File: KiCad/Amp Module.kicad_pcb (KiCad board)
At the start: 2 copper layers, 13.2 x 16.3 mm, 2 parts

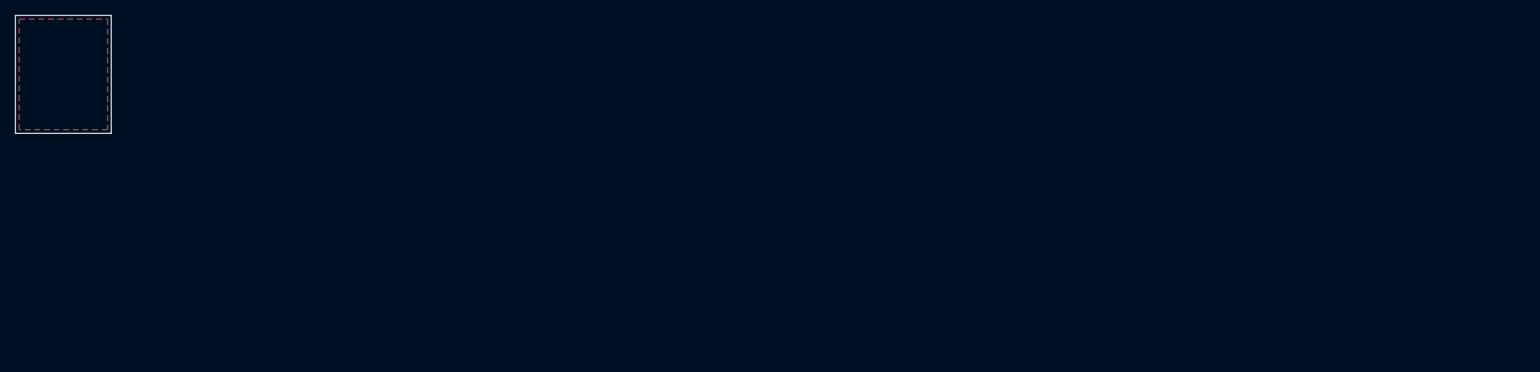
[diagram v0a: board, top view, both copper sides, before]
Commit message: finished PCB with TL12
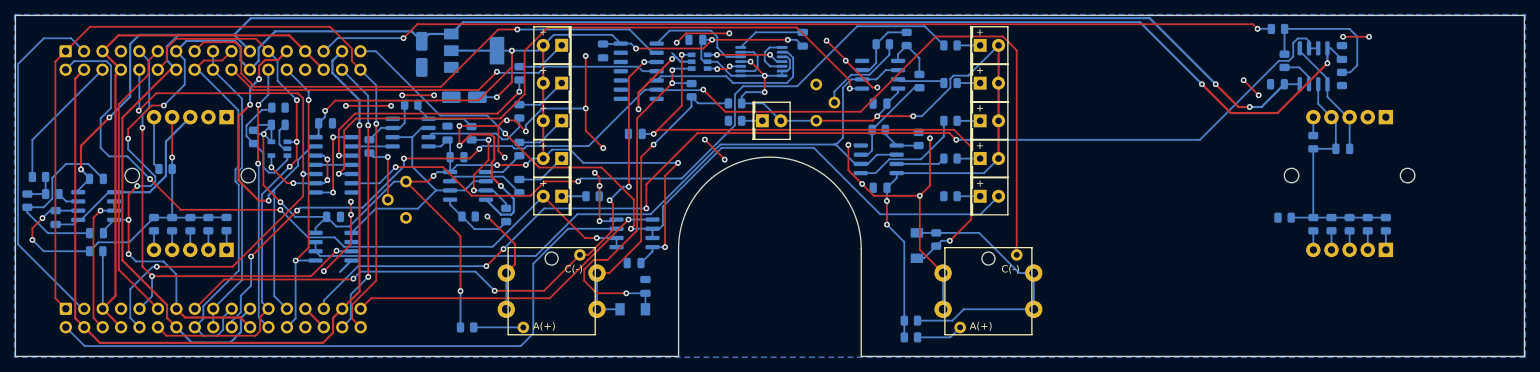
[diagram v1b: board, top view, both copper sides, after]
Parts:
- removed G***: LOGO, AmpModule:Fingerprint_SolderMask
- removed G***: LOGO, AmpModule:Fingerprint
- added C1: 22p, Capacitor_SMD:C_0805_2012Metric, B.Cu at (20.8, 43.1)
- added C10: 1u, Capacitor_SMD:C_0805_2012Metric, B.Cu at (100.7, 31.6)
- added C11: 0.1uF, Capacitor_SMD:C_0805_2012Metric, B.Cu at (100.5, 49.4)
- added C12: 0.1uF, Capacitor_SMD:C_0805_2012Metric, B.Cu at (123.8, 18.5)
- added C13: 0.1uF, Capacitor_SMD:C_0805_2012Metric, B.Cu at (96.2, 20.1)
- added C14: 0.1uF, Capacitor_SMD:C_0805_2012Metric, B.Cu at (51.5, 30.3)
- added C15: 0.1uF, Capacitor_SMD:C_0805_2012Metric, B.Cu at (59.1, 43.0)
- added C16: 0.1uF, Capacitor_SMD:C_0805_2012Metric, B.Cu at (58.0, 30.1)
- added C17: 0.1uF, Capacitor_SMD:C_0805_2012Metric, B.Cu at (74.8, 31.5)
- added C18: 0.1uF, Capacitor_SMD:C_0805_2012Metric, B.Cu at (76.1, 34.8)
- added C19: 0.1uF, Capacitor_SMD:C_0805_2012Metric, B.Cu at (134.4, 39.0)
- added C2: 22p, Capacitor_SMD:C_0805_2012Metric, B.Cu at (198.2, 33.6)
- added C20: 0.1uF, Capacitor_SMD:C_0805_2012Metric, B.Cu at (134.4, 27.4)
- added C21: 0.1uF, Capacitor_SMD:C_0805_2012Metric, B.Cu at (109.0, 18.6)
- added C3: 0.1uF, Capacitor_SMD:C_0805_2012Metric, B.Cu at (26.4, 37.8)
- added C4: 0.1uF, Capacitor_SMD:C_0805_2012Metric, B.Cu at (189.2, 24.7)
- added C5: 0.1uF, Capacitor_SMD:C_0805_2012Metric, B.Cu at (26.4, 45.3)
- added C6: 0.1uF, Capacitor_SMD:C_0805_2012Metric, B.Cu at (198.1, 20.4)
- added C7: 10uF, Capacitor_SMD:CP_Elec_4x5.3, B.Cu at (71.2, 20.6)
- added C8: 22uF, Capacitor_SMD:CP_Elec_4x5.3, B.Cu at (77.1, 26.5)
- added C9: 1u, Capacitor_SMD:C_0805_2012Metric, B.Cu at (102.1, 52.6)
- added D1: D_Small, Diode_SMD:D_MiniMELF, B.Cu at (100.3, 55.7)
- added D10: LED_Small, LED_THT:LED_Rectangular_W5.0mm_H5.0mm, F.Cu at (148.2, 24.6)
- added D11: LED_Small, LED_THT:LED_Rectangular_W5.0mm_H5.0mm, F.Cu at (148.2, 29.8)
- added D12: LED_Small, LED_THT:LED_Rectangular_W5.0mm_H5.0mm, F.Cu at (148.2, 35.0)
- added D13: LED_Small, LED_THT:LED_Rectangular_W5.0mm_H5.0mm, F.Cu at (148.2, 19.4)
- added D2: D_Small, Diode_SMD:D_MiniMELF, B.Cu at (139.5, 47.0)
- added D3: READY1, LED_THT:LED_Rectangular_W5.0mm_H5.0mm, F.Cu at (90.5, 40.2)
- added D4: READY2, LED_THT:LED_Rectangular_W5.0mm_H5.0mm, F.Cu at (148.2, 40.2)
- added D5: ON, LED_THT:LED_Rectangular_W5.0mm_H5.0mm, F.Cu at (118.2, 29.8)
- added D6: LED_Small, LED_THT:LED_Rectangular_W5.0mm_H5.0mm, F.Cu at (90.5, 24.6)
- added D7: LED_Small, LED_THT:LED_Rectangular_W5.0mm_H5.0mm, F.Cu at (90.5, 29.8)
- added D8: LED_Small, LED_THT:LED_Rectangular_W5.0mm_H5.0mm, F.Cu at (90.5, 35.0)
- added D9: LED_Small, LED_THT:LED_Rectangular_W5.0mm_H5.0mm, F.Cu at (90.5, 19.4)
- added J1: DSP, Connector_IDC:IDC-Header_2x17_P2.54mm_Vertical, B.Cu at (22.2, 20.2)
- added J2: LITEMOD, Connector_IDC:IDC-Header_2x17_P2.54mm_Vertical, B.Cu at (22.2, 55.7)
- added R1: 8.2k, Resistor_SMD:R_0805_2012Metric, B.Cu at (18.5, 37.5)
- added R10: 3.9k, Resistor_SMD:R_0805_2012Metric, B.Cu at (41.8, 44.0)
- added R11: 2.7k, Resistor_SMD:R_0805_2012Metric, B.Cu at (39.4, 44.0)
- added R12: 1.8k, Resistor_SMD:R_0805_2012Metric, B.Cu at (36.8, 44.0)
- added R13: 1k, Resistor_SMD:R_0805_2012Metric, B.Cu at (34.3, 44.0)
- added R14: 470, Resistor_SMD:R_0805_2012Metric, B.Cu at (35.9, 36.4)
- added R15: 5.36k, Resistor_SMD:R_0805_2012Metric, B.Cu at (204.1, 44.0)
- added R16: 3.9k, Resistor_SMD:R_0805_2012Metric, B.Cu at (201.6, 44.0)
- added R17: 2.7k, Resistor_SMD:R_0805_2012Metric, B.Cu at (199.1, 44.0)
- added R18: 1.8k, Resistor_SMD:R_0805_2012Metric, B.Cu at (196.6, 44.0)
- added R19: 1k, Resistor_SMD:R_0805_2012Metric, B.Cu at (194.1, 44.0)
- added R2: 8.2k, Resistor_SMD:R_0805_2012Metric, B.Cu at (189.3, 17.1)
- added R20: 470, Resistor_SMD:R_0805_2012Metric, B.Cu at (194.1, 32.7)
- added R21: 180, Resistor_SMD:R_0805_2012Metric, B.Cu at (77.5, 58.2)
- added R22: 180, Resistor_SMD:R_0805_2012Metric, B.Cu at (138.7, 59.6)
- added R23: 51k, Resistor_SMD:R_0805_2012Metric, B.Cu at (114.4, 27.4)
- added R24: 51k, Resistor_SMD:R_0805_2012Metric, B.Cu at (138.7, 57.3)
- added R25: 22k, Resistor_SMD:R_0805_2012Metric, B.Cu at (108.4, 25.5)
- added R26: 22k, Resistor_SMD:R_0805_2012Metric, B.Cu at (142.2, 46.1)
- added R27: 180, Resistor_SMD:R_0805_2012Metric, B.Cu at (94.8, 40.2)
- added R28: 180, Resistor_SMD:R_0805_2012Metric, B.Cu at (144.1, 40.2)
- added R29: 180, Resistor_SMD:R_0805_2012Metric, B.Cu at (114.4, 29.8)
- added R3: 2.7k, Resistor_SMD:R_0805_2012Metric, B.Cu at (16.9, 40.8)
- added R30: 120k, Resistor_SMD:R_0805_2012Metric, B.Cu at (48.1, 32.0)
- added R31: 39k, Resistor_SMD:R_0805_2012Metric, B.Cu at (51.5, 28.0)
- added R33: 6.8k, Resistor_SMD:R_0805_2012Metric, B.Cu at (64.0, 33.3)
- added R34: 12k, Resistor_SMD:R_0805_2012Metric, B.Cu at (69.8, 27.6)
- added R35: 27k, Resistor_SMD:R_0805_2012Metric, B.Cu at (78.1, 31.5)
- added R36: 18k, Resistor_SMD:R_0805_2012Metric, B.Cu at (82.9, 42.7)
- added R37: 56, Resistor_SMD:R_0805_2012Metric, B.Cu at (77.7, 43.0)
- added R38: 150, Resistor_SMD:R_0805_2012Metric, B.Cu at (84.7, 28.5)
- added R39: 150, Resistor_SMD:R_0805_2012Metric, B.Cu at (84.7, 33.7)
- added R4: 2.7k, Resistor_SMD:R_0805_2012Metric, B.Cu at (198.1, 24.0)
- added R40: 150, Resistor_SMD:R_0805_2012Metric, B.Cu at (84.7, 38.8)
- added R41: 150, Resistor_SMD:R_0805_2012Metric, B.Cu at (84.7, 23.2)
- added R43: 6.8k, Resistor_SMD:R_0805_2012Metric, B.Cu at (134.8, 19.2)
- added R44: 12k, Resistor_SMD:R_0805_2012Metric, B.Cu at (138.1, 18.5)
- added R45: 27k, Resistor_SMD:R_0805_2012Metric, B.Cu at (139.8, 24.3)
- added R46: 18k, Resistor_SMD:R_0805_2012Metric, B.Cu at (134.2, 31.0)
- added R47: 56, Resistor_SMD:R_0805_2012Metric, B.Cu at (139.7, 32.3)
- added R48: 150, Resistor_SMD:R_0805_2012Metric, B.Cu at (144.1, 24.6)
- added R49: 150, Resistor_SMD:R_0805_2012Metric, B.Cu at (144.1, 29.8)
- added R5: 1k, Resistor_SMD:R_0805_2012Metric, B.Cu at (20.3, 39.9)
- added R50: 150, Resistor_SMD:R_0805_2012Metric, B.Cu at (144.1, 35.0)
- added R51: 150, Resistor_SMD:R_0805_2012Metric, B.Cu at (144.1, 19.4)
- added R6: 1k, Resistor_SMD:R_0805_2012Metric, B.Cu at (190.2, 21.5)
- added R7: 1.8k, Resistor_SMD:R_0805_2012Metric, B.Cu at (26.4, 47.7)
- added R8: 1.8k, Resistor_SMD:R_0805_2012Metric, B.Cu at (190.2, 43.1)
- added R9: 5.36k, Resistor_SMD:R_0805_2012Metric, B.Cu at (44.3, 44.0)
- added RS1: Alps SRBV170701, AmpModule:Alps_SRBV170701, F.Cu at (39.3, 38.4)
- added RS2: Alps SRBV170701, AmpModule:Alps_SRBV170701, F.Cu at (199.1, 38.4)
- added RV1: 500k, AmpModule:Trim_audio, B.Cu at (69.1, 38.1)
- added RV2: 500k, AmpModule:Trim_audio, B.Cu at (125.6, 29.8)
- added SW1: MUTE1, AmpModule:Button, F.Cu at (89.2, 53.3)
- added SW2: MUTE2, AmpModule:Button, F.Cu at (149.4, 53.3)
- added U1: NE5532, Package_SO:SOIC-8_3.9x4.9mm_P1.27mm, B.Cu at (26.4, 41.5)
- added U11: LM393, Package_SO:SOIC-8_3.9x4.9mm_P1.27mm, B.Cu at (69.7, 31.4)
- added U12: LM393, Package_SO:SOIC-8_3.9x4.9mm_P1.27mm, B.Cu at (77.6, 38.7)
- added U13: 74HC08, Package_SO:SOIC-14_3.9x8.7mm_P1.27mm, B.Cu at (59.1, 35.8)
- added U14: LM393, Package_SO:SOIC-8_3.9x4.9mm_P1.27mm, B.Cu at (134.4, 23.4)
- added U15: LM393, Package_SO:SOIC-8_3.9x4.9mm_P1.27mm, B.Cu at (134.2, 35.1)
- added U2: NE5532, Package_SO:SOIC-8_3.9x4.9mm_P1.27mm, B.Cu at (194.2, 22.3)
- added U3: AMS1117-5.0, Package_TO_SOT_SMD:SOT-223-3_TabPin2, B.Cu at (78.5, 20.1)
- added U4: TL072, Package_SO:SOIC-8_3.9x4.9mm_P1.27mm, B.Cu at (100.6, 45.3)
- added U5: 74LVC2G14, Package_TO_SOT_SMD:SOT-23-6, B.Cu at (109.6, 21.6)
- added U6: 74VHC74, Package_SO:TSSOP-14_4.4x5mm_P0.65mm, B.Cu at (118.1, 21.6)
- added U7: 74HC08, Package_SO:SOIC-14_3.9x8.7mm_P1.27mm, B.Cu at (101.2, 22.9)
- added U8: LMV321, Package_TO_SOT_SMD:SOT-23-5, B.Cu at (51.6, 33.6)
- added U9: TL072, Package_SO:SOIC-8_3.9x4.9mm_P1.27mm, B.Cu at (59.1, 47.1)
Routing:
- net +5V_REG: track 0.00 -> 378.0 mm, vias 0 -> 21
- net GND: track 0.00 -> 317.8 mm, vias 0 -> 37
- net -12VDC: track 0.00 -> 258.8 mm, vias 0 -> 4
- net +12VDC: track 0.00 -> 244.6 mm, vias 0 -> 7
- net LM_MUTE2: track 0.00 -> 161.4 mm, vias 0 -> 5
- net LM_IN2+: track 0.00 -> 158.1 mm, vias 0 -> 4
- net DSP_OUT2+: track 0.00 -> 132.5 mm, vias 0 -> 2
- net SDPWS: track 0.00 -> 120.5 mm, vias 0 -> 1
- net +5VDC: track 0.00 -> 114.7 mm, vias 0 -> 1
- net READY_DSP2: track 0.00 -> 113.2 mm, vias 0 -> 2
- net Net-(U14-Pad2): track 0.00 -> 106.7 mm
- net READY_DSP1: track 0.00 -> 102.2 mm, vias 0 -> 3
- net Net-(R51-Pad2): track 0.00 -> 97.5 mm, vias 0 -> 2
- net Net-(U13-Pad5): track 0.00 -> 93.1 mm, vias 0 -> 2
- net LM_MUTE1: track 0.00 -> 91.8 mm, vias 0 -> 5
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- added copper zone on B.Cu, net GND
- removed copper zone on F.Cu, net (none)
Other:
- board size 13.2 x 16.3 mm -> 208 x 47 mm
- board text added: "+"

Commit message: changed to TL2
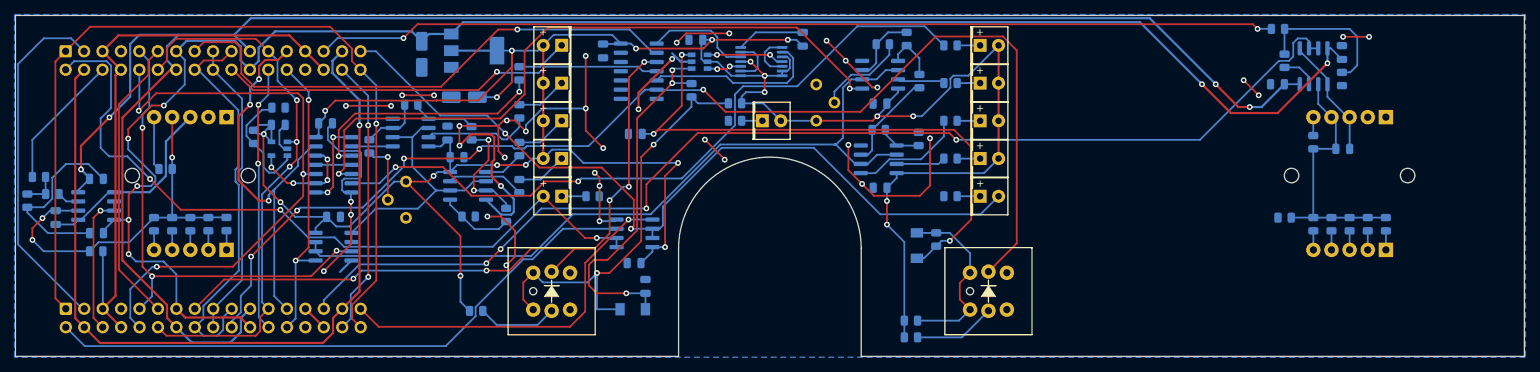
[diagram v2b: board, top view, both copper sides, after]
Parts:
- SW1, SW2: footprint AmpModule:Button -> AmpModule:TL2-NNS7
- moved R21 2.59 mm to (78.7, 56.0)
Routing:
- net Net-(D1-Pad2): track 44.3 -> 60.4 mm, vias 1 -> 2
- net Net-(D2-Pad2): track 40.1 -> 25.3 mm
- net READY2: track 45.3 -> 51.3 mm
- net READY1: track 89.3 -> 84.4 mm
- net Net-(R22-Pad2): track 6.43 -> 11.3 mm
- net LM_MUTE1: track 91.8 -> 96.5 mm
- net Net-(R21-Pad2): track 6.84 -> 11.1 mm
- net GND: track 317.8 -> 313.8 mm
- net LM_MUTE2: track 161.4 -> 165.3 mm
- net +5V_REG: track 378.0 -> 376.3 mm
- net Net-(C9-Pad1): track 52.0 -> 51.4 mm

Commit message: corrected rotary switch footprint
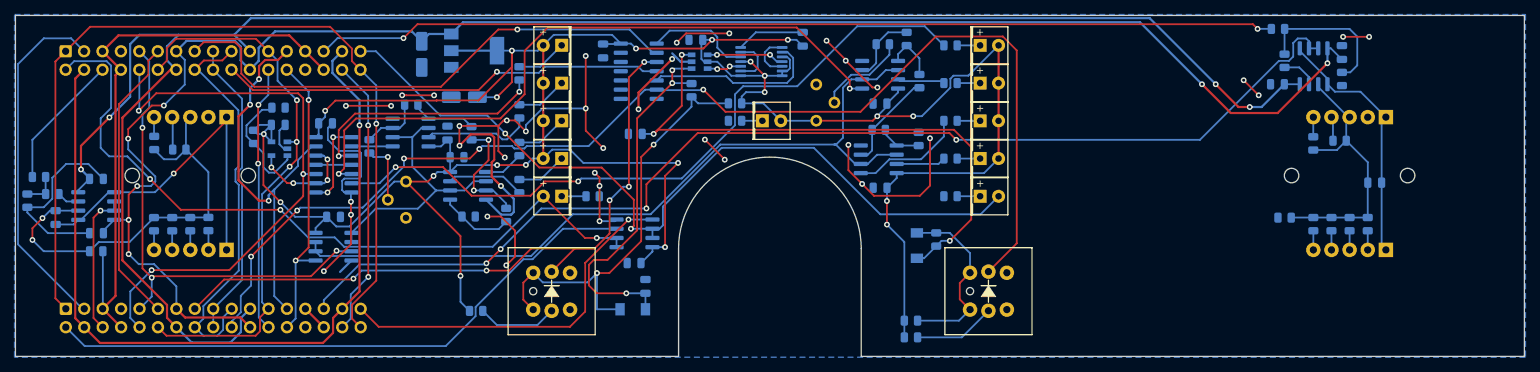
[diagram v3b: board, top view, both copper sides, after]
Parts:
- removed RS1, RS2: Alps SRBV170701, AmpModule:Alps_SRBV170701
- added U10: Alps_SRBV170701, AmpModule:Alps_SRBV170701, F.Cu at (39.3, 38.4)
- added U16: Alps_SRBV170701, AmpModule:Alps_SRBV170701, F.Cu at (199.1, 38.4)
- moved R13 11.2 mm to (34.4, 32.8), turned to 90 degrees
- moved R19 11.1 mm to (194.1, 32.9), turned to 90 degrees
- moved C2 6.41 mm to (202.6, 38.3)
- moved R20 3.64 mm to (197.8, 32.5), turned to 180 degrees
- moved R14 3.28 mm to (37.8, 33.7)
- moved R15 2.50 mm to (201.6, 44.0)
- moved R16 2.50 mm to (199.1, 44.0)
- moved R17 2.50 mm to (196.6, 44.0)
- moved R18 2.50 mm to (194.1, 44.0)
- moved R10 2.50 mm to (39.3, 44.0)
- moved R11 2.50 mm to (36.9, 44.0)
- moved R12 2.50 mm to (34.3, 44.0)
- moved R9 2.50 mm to (41.8, 44.0)
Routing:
- net Net-(C1-Pad1): track 27.5 -> 48.3 mm, vias 0 -> 1
- net Net-(C2-Pad1): track 16.9 -> 35.3 mm
- net Net-(C1-Pad2): track 52.1 -> 56.6 mm, vias 3 -> 2
- net Net-(R14-Pad2): track 7.43 -> 4.50 mm
- net Net-(C2-Pad2): track 35.6 -> 37.3 mm
- net +12VDC: track 244.6 -> 243.7 mm
- net Net-(R20-Pad2): track 2.55 -> 3.34 mm

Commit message: started BOM export
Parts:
- renumbered C21 to C12, C12 to C13, C13 to C14, C18 to C15, C19 to C16, C20 to C17, C14 to C18, C15 to C19, C16 to C20, C17 to C21, R33 to R32, R34 to R33, R35 to R34, R36 to R35, R37 to R36, R38 to R37, R39 to R38, R40 to R39, R41 to R40, R43 to R41, R44 to R42, R45 to R43, R46 to R44, R47 to R45, R48 to R46, R49 to R47, R50 to R48, R51 to R49, U10 to SW1, U16 to SW2, SW1 to SW3, SW2 to SW4, U11 to U10, U8 to U11, U14 to U13, U15 to U14, U13 to U8
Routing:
- net Net-(C9-Pad1): track 51.4 -> 46.6 mm
- net Net-(D1-Pad2): track 60.4 -> 57.8 mm
- net GND: track 313.8 -> 312.9 mm

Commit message: exported BOM and pos
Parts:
- R15, R9: value 5.36k -> 5.6k
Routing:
- net GND: track 312.9 -> 311.8 mm
- net LM_MUTE1: track 96.5 -> 95.9 mm

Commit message: exported gerbers and all JLC files
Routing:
- net GND: track 311.8 -> 293.7 mm
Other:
- rule pad_to_mask_clearance: 0.05 -> 0

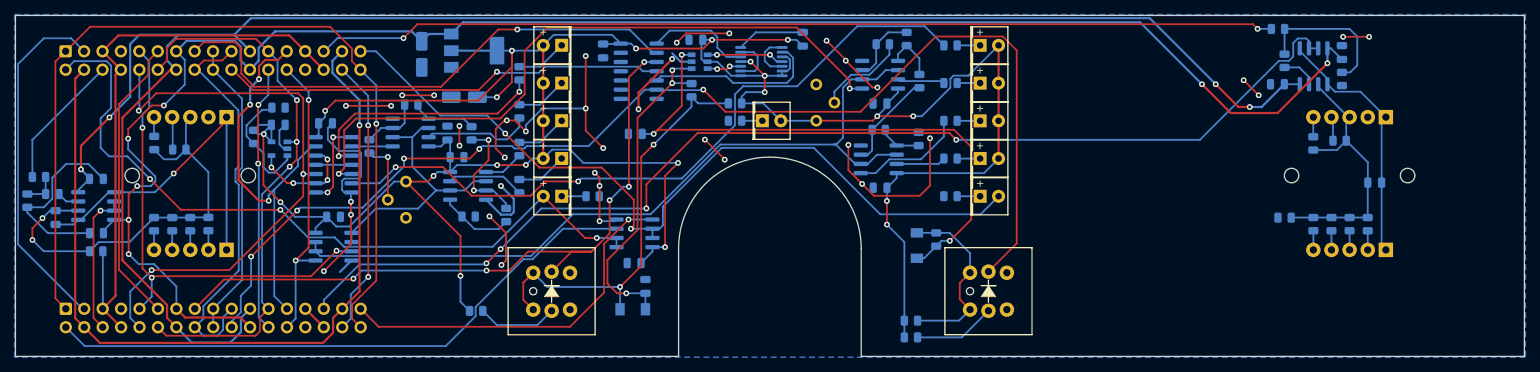
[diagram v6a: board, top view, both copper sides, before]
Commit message: moved some traces
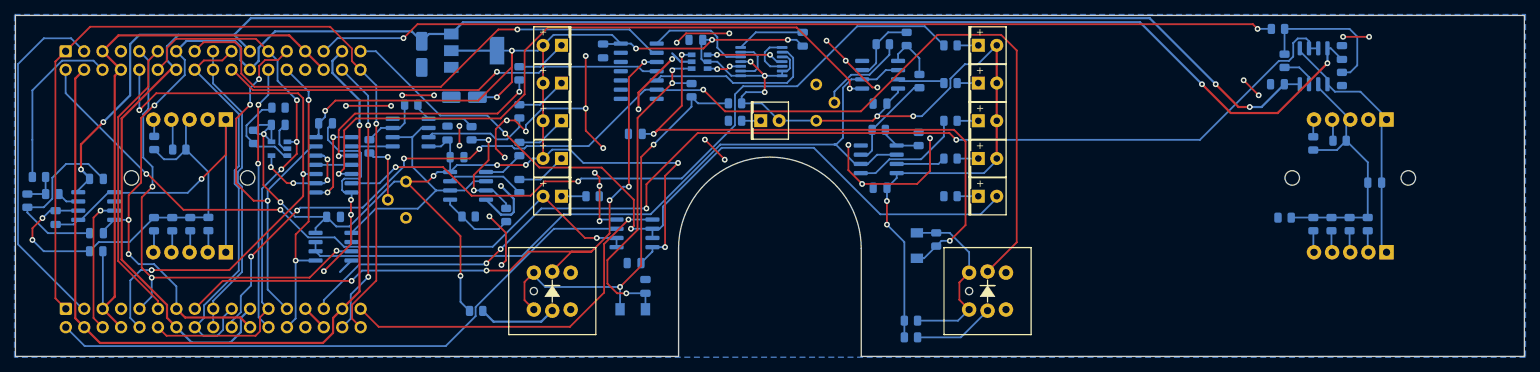
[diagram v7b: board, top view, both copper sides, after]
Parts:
- moved SW1 0.35 mm to (39.2, 38.7)
- moved SW2 0.34 mm to (199.2, 38.7)
- moved D10 0.25 mm to (148.0, 24.6)
- moved D11 0.25 mm to (148.0, 29.8)
- moved D12 0.25 mm to (148.0, 35.0)
- moved D13 0.25 mm to (148.0, 19.4)
- moved D4 0.25 mm to (148.0, 40.2)
- moved D5 0.23 mm to (118.0, 29.7)
- moved SW4 0.13 mm to (149.2, 53.2)
- moved SW3 0.09 mm to (89.2, 53.2)
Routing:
- net READY_DSP1: track 102.2 -> 94.5 mm
- net +12VDC: track 243.7 -> 238.5 mm, vias 7 -> 5
- net DSP_OUT1+: track 18.8 -> 23.8 mm
- net Net-(R30-Pad2): track 16.2 -> 12.7 mm
- net Net-(C1-Pad1): track 48.3 -> 51.1 mm
- net GND: track 293.7 -> 291.1 mm
- net Net-(C2-Pad1): track 35.3 -> 37.4 mm
- net VOUT1MON: track 66.8 -> 68.1 mm
- net PROTECT1: track 79.6 -> 80.7 mm
- net Net-(C10-Pad1): track 80.1 -> 79.5 mm
- net PROTECT2: track 54.5 -> 54.0 mm

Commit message: rotated LEDs and cutted PCB
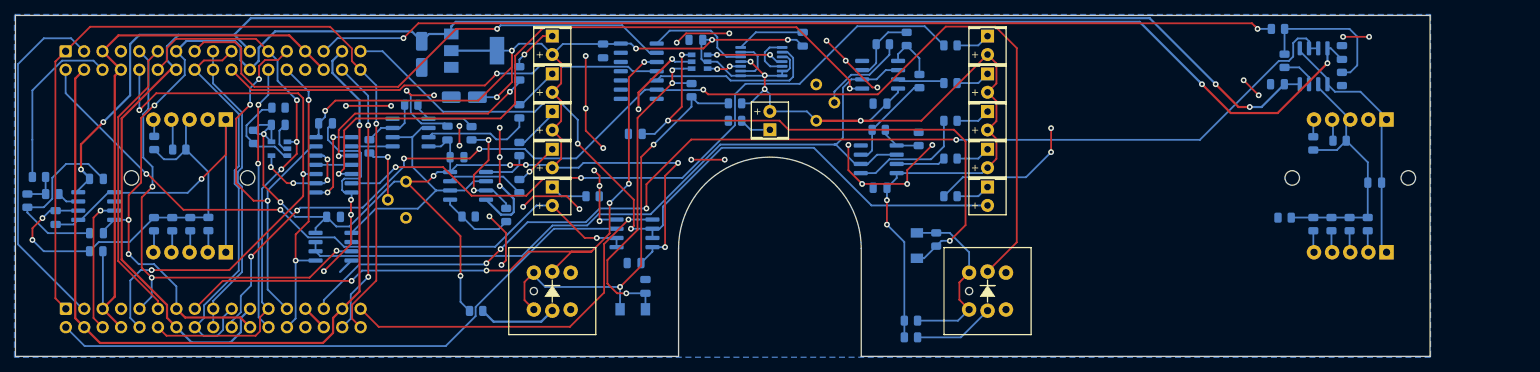
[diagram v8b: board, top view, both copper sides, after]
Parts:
- moved D4 1.80 mm to (149.2, 38.9), turned to 270 degrees
- moved Deee 1.80 mm to (89.2, 38.9), turned to 270 degrees
- moved D10 1.80 mm to (149.2, 23.3), turned to 270 degrees
- moved D11 1.80 mm to (149.2, 28.5), turned to 270 degrees
- moved D13 1.80 mm to (149.2, 18.1), turned to 270 degrees
- moved D6 1.80 mm to (89.2, 23.3), turned to 270 degrees
- moved D7 1.80 mm to (89.2, 28.5), turned to 270 degrees
- moved D9 1.80 mm to (89.2, 18.1), turned to 270 degrees
- moved D12 1.80 mm to (149.2, 33.7), turned to 270 degrees
- moved D8 1.80 mm to (89.2, 33.7), turned to 270 degrees
- moved D5 1.80 mm to (119.2, 31.0), turned to 90 degrees
- renumbered D3 to Deee
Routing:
- net GND: track 291.1 -> 317.0 mm, vias 37 -> 41
- net +5V_REG: track 376.1 -> 382.5 mm, vias 21 -> 20
- net Net-(D3-Pad1): track 3.36 -> 5.18 mm
- net Net-(D11-Pad1): track 2.93 -> 4.72 mm
- net Net-(D10-Pad1): track 2.93 -> 4.72 mm
- net Net-(D13-Pad1): track 2.93 -> 4.72 mm
- net Net-(D12-Pad1): track 2.94 -> 4.72 mm
- net Net-(D4-Pad1): track 2.93 -> 4.72 mm
- net Net-(D5-Pad1): track 2.64 -> 4.41 mm
- net Net-(C10-Pad1): track 79.5 -> 77.9 mm
- net READY_DSP1: track 94.5 -> 93.4 mm
- net Net-(R47-Pad2): track 15.7 -> 16.5 mm
- net Net-(D8-Pad1): track 7.03 -> 6.26 mm, vias 0 -> 1
- net Net-(D6-Pad1): track 7.06 -> 6.30 mm
- net Net-(R40-Pad2): track 34.1 -> 33.4 mm
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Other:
- board size 208 x 47 mm -> 195 x 47 mm
